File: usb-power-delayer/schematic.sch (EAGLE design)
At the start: 8 parts, among them Q1 BC547B, Q3 BS250

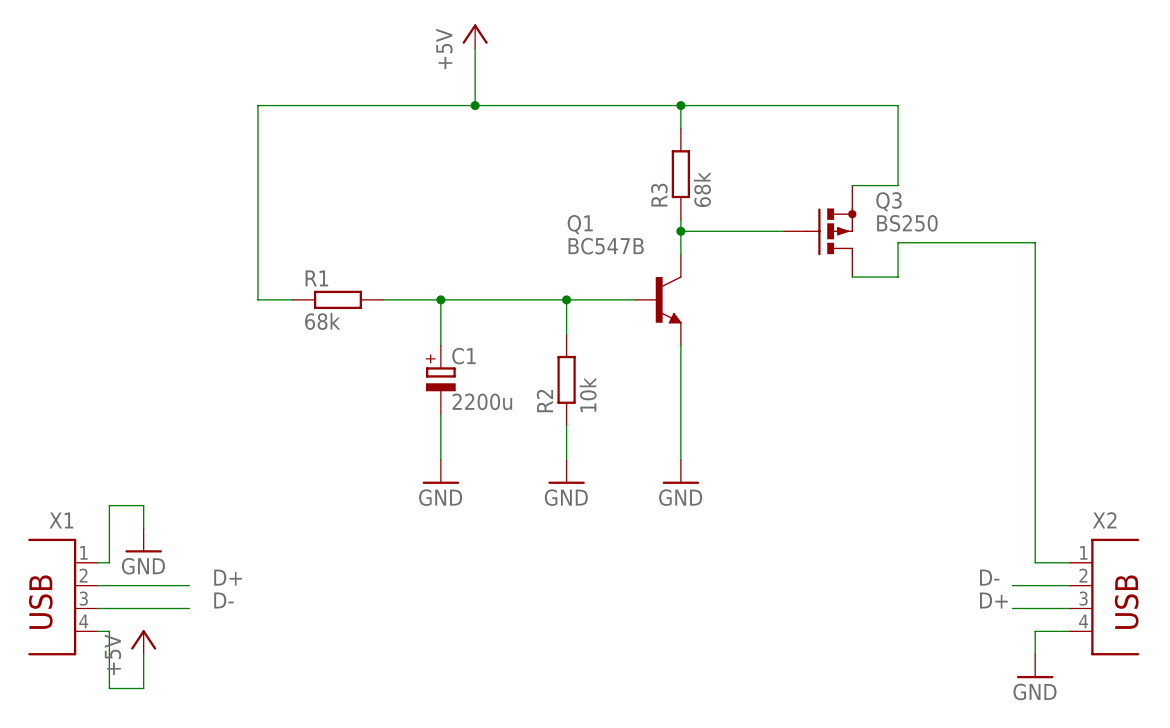
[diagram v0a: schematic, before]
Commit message: [USB-Delayer] Extend the delay time from ~35s to ~52s as 35s was sometimes not enough.
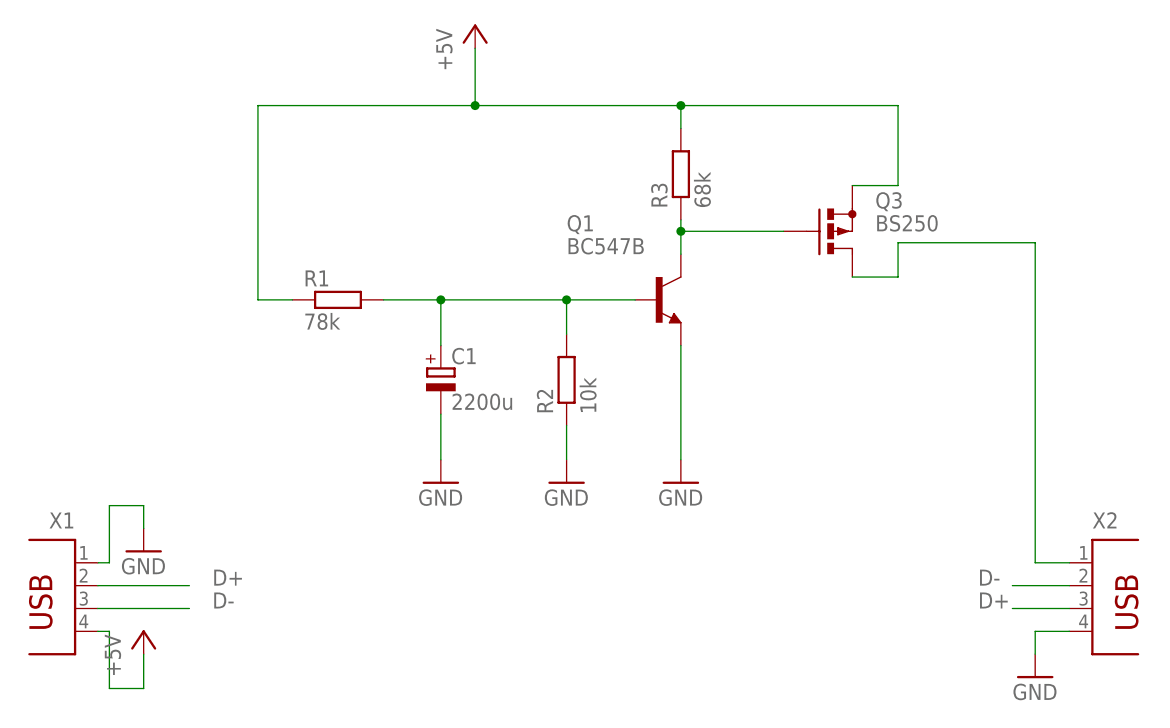
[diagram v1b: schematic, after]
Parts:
- R1: value 68k -> 78k
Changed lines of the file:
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@@
 <grid distance="0.05" unitdist="inch" unit="inch" style="lines" multiple="1" display="no" altdistance="0.01" altunitdist="inch" altunit="inch"/>
 <layers>
-<layer number="1" name="Top" color="4" fill="1" visible="yes" active="no"/>
-<layer number="16" name="Bottom" color="1" fill="1" visible="yes" active="no"/>
-<layer number="17" name="Pads" color="2" fill="1" visible="yes" active="no"/>
-<layer number="18" name="Vias" color="2" fill="1" visible="yes" active="no"/>
-<layer number="19" name="Unrouted" color="6" fill="1" visible="yes" active="no"/>
-<layer number="20" name="Dimension" color="24" fill="1" visible="yes" active="no"/>
-<layer number="21" name="tPlace" color="7" fill="1" visible="yes" active="no"/>
-<layer number="22" name="bPlace" color="7" fill="1" visible="yes" active="no"/>
-<layer number="23" name="tOrigins" color="15" fill="1" visible="yes" active="no"/>
-<layer number="24" name="bOrigins" color="15" fill="1" visible="yes" active="no"/>
-<layer number="25" name="tNames" color="7" fill="1" visible="yes" active="no"/>
-<layer number="26" name="bNames" color="7" fill="1" visible="yes" active="no"/>
-<layer number="27" name="tValues" color="7" fill="1" visible="yes" active="no"/>
-<layer number="28" name="bValues" color="7" fill="1" visible="yes" active="no"/>
+<layer number="1" name="Top" color="4" fill="1" visible="no" active="no"/>
+<layer number="16" name="Bottom" color="1" fill="1" visible="no" active="no"/>
+<layer number="17" name="Pads" color="2" fill="1" visible="no" active="no"/>
+<layer number="18" name="Vias" color="2" fill="1" visible="no" active="no"/>
+<layer number="19" name="Unrouted" color="6" fill="1" visible="no" active="no"/>
+<layer number="20" name="Dimension" color="24" fill="1" visible="no" active="no"/>
+<layer number="21" name="tPlace" color="7" fill="1" visible="no" active="no"/>
+<layer number="22" name="bPlace" color="7" fill="1" visible="no" active="no"/>
+<layer number="23" name="tOrigins" color="15" fill="1" visible="no" active="no"/>
+<layer number="24" name="bOrigins" color="15" fill="1" visible="no" active="no"/>
+<layer number="25" name="tNames" color="7" fill="1" visible="no" active="no"/>
+<layer number="26" name="bNames" color="7" fill="1" visible="no" active="no"/>
+<layer number="27" name="tValues" color="7" fill="1" visible="no" active="no"/>
+<layer number="28" name="bValues" color="7" fill="1" visible="no" active="no"/>
 <layer number="29" name="tStop" color="7" fill="3" visible="no" active="no"/>
 <layer number="30" name="bStop" color="7" fill="6" visible="no" active="no"/>
@@
 <layer number="35" name="tGlue" color="7" fill="4" visible="no" active="no"/>
 <layer number="36" name="bGlue" color="7" fill="5" visible="no" active="no"/>
-<layer number="37" name="tTest" color="7" fill="1" visible="yes" active="no"/>
-<layer number="38" name="bTest" color="7" fill="1" visible="yes" active="no"/>
+<layer number="37" name="tTest" color="7" fill="1" visible="no" active="no"/>
+<layer number="38" name="bTest" color="7" fill="1" visible="no" active="no"/>
 <layer number="39" name="tKeepout" color="4" fill="11" visible="no" active="no"/>
 <layer number="40" name="bKeepout" color="1" fill="11" visible="no" active="no"/>
@@
 <layer number="44" name="Drills" color="7" fill="1" visible="no" active="no"/>
 <layer number="45" name="Holes" color="7" fill="1" visible="no" active="no"/>
-<layer number="46" name="Milling" color="3" fill="1" visible="yes" active="no"/>
-<layer number="47" name="Measures" color="7" fill="1" visible="yes" active="no"/>
-<layer number="48" name="Document" color="7" fill="1" visible="yes" active="no"/>
-<layer number="49" name="Reference" color="7" fill="1" visible="yes" active="no"/>
-<layer number="51" name="tDocu" color="7" fill="1" visible="yes" active="no"/>
-<layer number="52" name="bDocu" color="7" fill="1" visible="yes" active="no"/>
+<layer number="46" name="Milling" color="3" fill="1" visible="no" active="no"/>
+<layer number="47" name="Measures" color="7" fill="1" visible="no" active="no"/>
+<layer number="48" name="Document" color="7" fill="1" visible="no" active="no"/>
+<layer number="49" name="Reference" color="7" fill="1" visible="no" active="no"/>
+<layer number="51" name="tDocu" color="7" fill="1" visible="no" active="no"/>
+<layer number="52" name="bDocu" color="7" fill="1" visible="no" active="no"/>
 <layer number="88" name="SimResults" color="9" fill="1" visible="yes" active="yes"/>
 <layer number="89" name="SimProbes" color="9" fill="1" visible="yes" active="yes"/>
@@
 </classes>
 <parts>
-<part name="R1" library="rcl" library_urn="urn:adsk.eagle:library:334" deviceset="R-EU_" device="0204/5" package3d_urn="urn:adsk.eagle:package:23488/1" value="68k"/>
+<part name="R1" library="rcl" library_urn="urn:adsk.eagle:library:334" deviceset="R-EU_" device="0204/5" package3d_urn="urn:adsk.eagle:package:23488/1" value="78k"/>
 <part name="R2" library="rcl" library_urn="urn:adsk.eagle:library:334" deviceset="R-EU_" device="0204/5" package3d_urn="urn:adsk.eagle:package:23488/1" value="10k"/>
 <part name="R3" library="rcl" library_urn="urn:adsk.eagle:library:334" deviceset="R-EU_" device="0204/5" package3d_urn="urn:adsk.eagle:package:23488/1" value="68k"/>
